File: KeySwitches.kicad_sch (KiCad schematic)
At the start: 8 parts, among them K1 SW_Push, K2 SW_Push, K3 SW_Push, K4 SW_Push

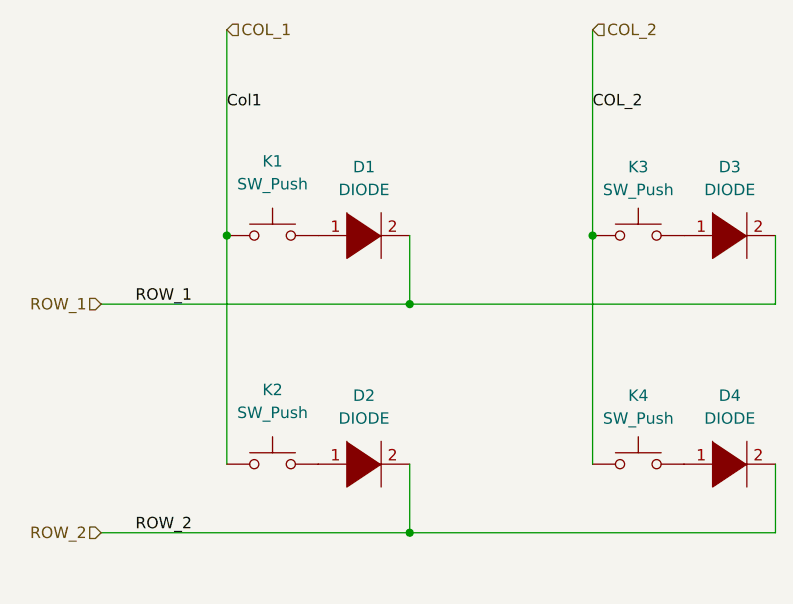
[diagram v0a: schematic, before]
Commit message: WIP: Updated SK6812Mini to SK6812Mini-E and remapped ref des keys between PCB and Schematic.
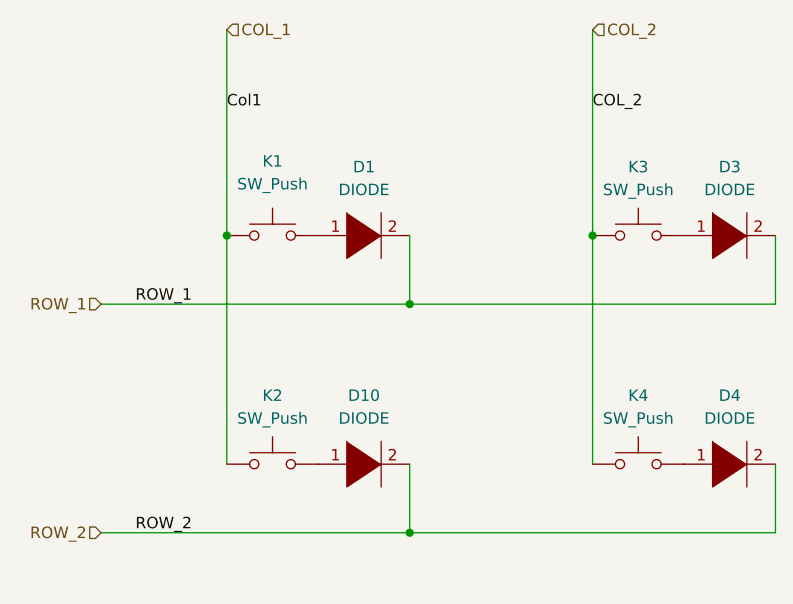
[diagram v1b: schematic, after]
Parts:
- renumbered D2 to D10
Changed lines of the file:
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@@
 		(fields_autoplaced yes)
 		(property "Reference" "K2"
-			(at 50.8 65.405 0)
+			(at 50.8 66.04 0)
 			(effects
 				(font
@@
 		)
 		(property "Value" "SW_Push"
-			(at 50.8 67.945 0)
+			(at 50.8 68.58 0)
 			(effects
 				(font
@@
 		(on_board yes)
 		(dnp no)
-		(property "Reference" "D2"
+		(property "Reference" "D10"
 			(at 60.96 66.04 0)
 			(effects
@@
 			(project "cheapino"
 				(path "/4e0ee48d-0121-4621-a533-4795bdfb88f1/102c4ac7-9dfb-411a-bce5-c6035c42c9ce"
-					(reference "D2")
+					(reference "D10")
 					(unit 1)
 				)

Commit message: Placing nearly all components onto the PCB. Removing the 9Vto5V battery input stage from populating onto the PCB.
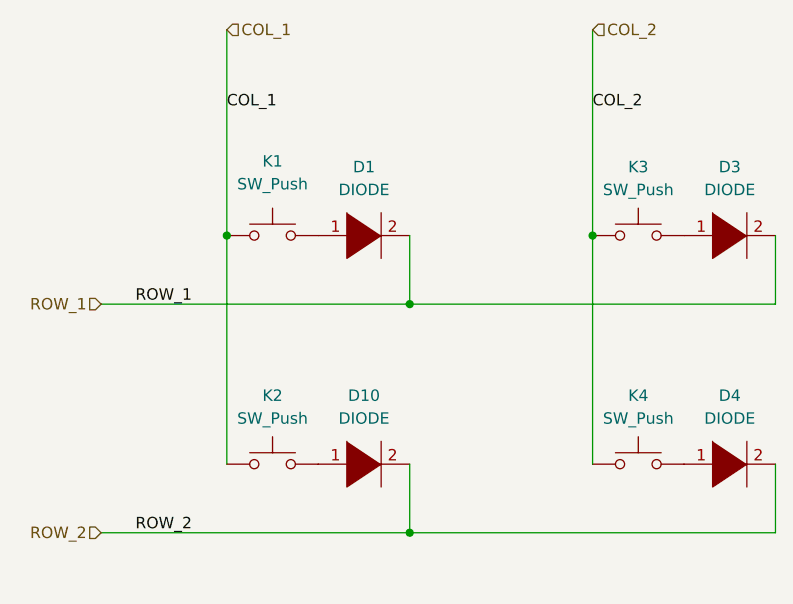
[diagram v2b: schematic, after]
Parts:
- D1, D10, D3, D4: footprint keebio:Diode-dual -> Keebio-Parts:Diode-dual
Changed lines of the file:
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@@
 		)
 	)
-	(label "Col1"
+	(label "COL_1"
 		(at 45.72 34.29 0)
 		(fields_autoplaced yes)
@@
 			)
 		)
-		(property "Footprint" "keebio:Diode-dual"
+		(property "Footprint" "Keebio-Parts:Diode-dual"
 			(at 101.6 73.66 0)
 			(effects
@@
 			)
 		)
-		(property "Footprint" "keebio:Diode-dual"
+		(property "Footprint" "Keebio-Parts:Diode-dual"
 			(at 101.6 48.26 0)
 			(effects
@@
 			)
 		)
-		(property "Footprint" "keebio:Diode-dual"
+		(property "Footprint" "Keebio-Parts:Diode-dual"
 			(at 60.96 48.26 0)
 			(effects
@@
 			)
 		)
-		(property "Footprint" "keebio:Diode-dual"
+		(property "Footprint" "Keebio-Parts:Diode-dual"
 			(at 60.96 73.66 0)
 			(effects

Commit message: Added testpoints, finished placing components, fixed footprint mapping, and ready to start routing tracks.
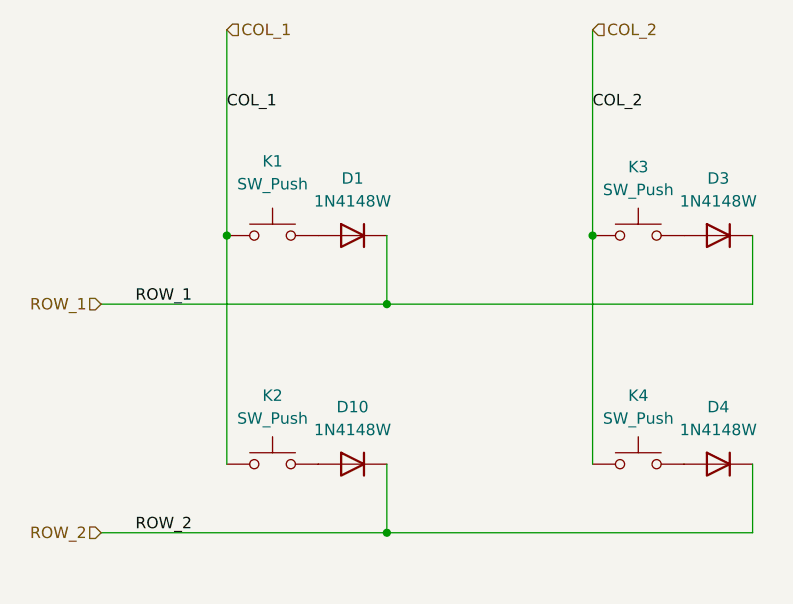
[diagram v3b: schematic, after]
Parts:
- removed D1, D10, D3, D4: DIODE, Keebio-Parts:Diode-dual, symbol pspice:DIODE
- added D1, D10, D3, D4: 1N4148W, Keebio-Parts:Diode-dual, symbol Diode:1N4148W
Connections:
- net ROW_1: now also D1.1 (K), D3.1 (K)
- net ROW_2: now also D10.1 (K), D4.1 (K)
- net at K1.2: now also D1.2 (A)
- net at K3.2: now also D3.2 (A)
- net at K4.2: now also D4.2 (A)
- net at K2.2: now also D10.2 (A)

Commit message: Adding additional LEDs and driver to test per-key LEDs, updating net classes and design constraints, and starting to route tracks.
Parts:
- K2, K4: footprint keyswitches:Kailh_socket_MX_optional_reversible -> keyswitches:Kailh_socket_MX
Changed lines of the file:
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@@
 			)
 		)
-		(property "Footprint" "keyswitches:Kailh_socket_MX_optional_reversible"
+		(property "Footprint" "keyswitches:Kailh_socket_MX"
 			(at 91.44 68.58 0)
 			(effects
@@
 			)
 		)
-		(property "Footprint" "keyswitches:Kailh_socket_MX_optional_reversible"
+		(property "Footprint" "keyswitches:Kailh_socket_MX"
 			(at 50.8 68.58 0)
 			(effects

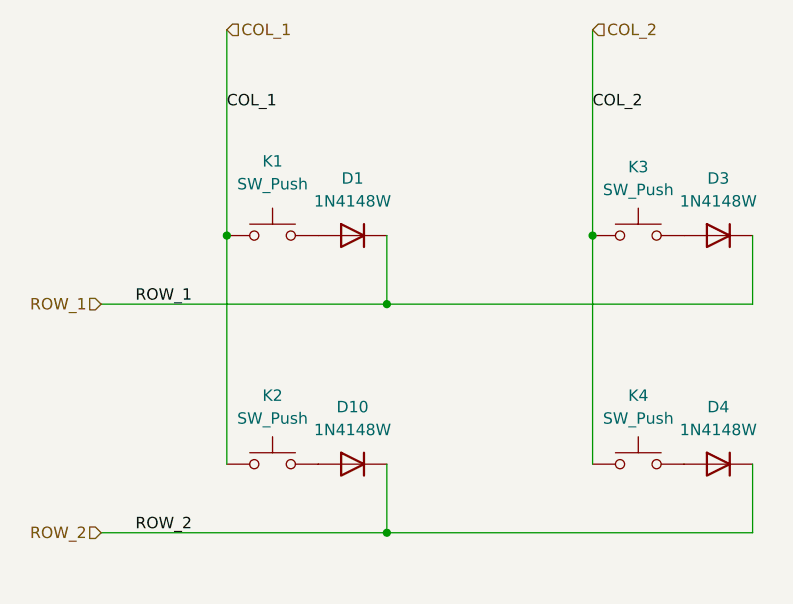
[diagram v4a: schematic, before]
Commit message: Shrinking board to only have 2 key switches and a few other unnecessary components. Finished with routing the rest of the board.
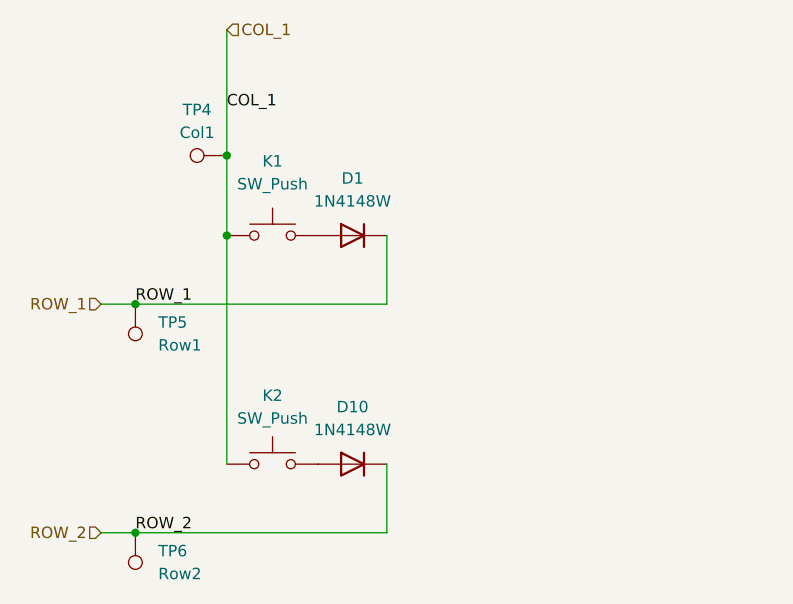
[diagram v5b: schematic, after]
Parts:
- removed D3, D4: 1N4148W, Keebio-Parts:Diode-dual, symbol Diode:1N4148W
- removed K3: SW_Push, keyswitches:Kailh_socket_MX_optional_reversible, symbol Switch:SW_Push
- removed K4: SW_Push, keyswitches:Kailh_socket_MX, symbol Switch:SW_Push
- added TP4: Col1, TestPoint:TestPoint_Pad_D1.5mm, symbol Connector:TestPoint
- added TP5: Row1, TestPoint:TestPoint_Pad_D1.5mm, symbol Connector:TestPoint
- added TP6: Row2, TestPoint:TestPoint_Pad_D1.5mm, symbol Connector:TestPoint
- D1, D10: footprint Keebio-Parts:Diode-dual -> Diode_SMD:D_SOD-123
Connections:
- net COL_1: now also TP4.1
- net ROW_1: now also TP5.1
- net ROW_2: now also TP6.1
